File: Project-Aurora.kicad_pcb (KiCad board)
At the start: 4 copper layers, 285 x 94.6 mm, 252 parts, among them P1 USB_OTG, P2 FLASH_HDR, SW1 Reset, SW10 SW_PUSH, SW11 SW_PUSH, SW12 SW_PUSH, SW13 SW_PUSH, SW14 SW_PUSH, SW15 SW_PUSH, SW16 SW_PUSH, SW17 SW_PUSH, SW18 SW_PUSH, SW19 SW_PUSH, SW2 SW_PUSH, SW20 SW_PUSH, SW21 SW_PUSH, SW22 SW_PUSH, SW23 SW_PUSH, SW24 SW_PUSH, SW25 SW_PUSH, SW26 SW_PUSH, SW27 SW_PUSH, SW28 SW_PUSH, SW29 SW_PUSH, SW3 SW_PUSH, SW30 SW_PUSH, SW31 SW_PUSH, SW32 SW_PUSH, SW33 SW_PUSH, SW34 SW_PUSH, SW35 SW_PUSH, SW36 SW_PUSH, SW37 SW_PUSH, SW38 SW_PUSH, SW39 SW_PUSH, SW4 SW_PUSH, SW40 SW_PUSH, SW41 SW_PUSH, SW42 SW_PUSH, SW43 SW_PUSH, SW44 SW_PUSH, SW45 SW_PUSH, SW46 SW_PUSH, SW47 SW_PUSH, SW48 SW_PUSH, SW49 SW_PUSH, SW5 SW_PUSH, SW50 SW_PUSH, SW51 SW_PUSH, SW52 SW_PUSH, SW53 SW_PUSH, SW54 SW_PUSH, SW55 SW_PUSH, SW56 SW_PUSH, SW57 SW_PUSH, SW58 SW_PUSH, SW59 SW_PUSH, SW6 SW_PUSH, SW60 SW_PUSH, SW61 SW_PUSH, SW62 SW_PUSH, SW63 SW_PUSH, SW64 SW_PUSH, SW65 SW_PUSH, SW66 SW_PUSH, SW7 SW_PUSH, SW8 SW_PUSH, SW9 SW_PUSH, U1 IS31FL3732, U2 Freescale_K20P64M72SF1, U3 TPS62086, U5 IS31FL3732, U6 Case-Ground, X1 CRYSTAL_SMD

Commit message: Optimised Routing of Ground Trace
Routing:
- net GND: track 340.4 -> 322.8 mm, vias 37 -> 36
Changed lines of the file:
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@@
     (links 613)
     (no_connects 0)
-    (area 62.241349 64.570349 347.341251 159.269751)
+    (area -446.689481 14.894801 665.190441 593.940901)
     (thickness 1.6002)
     (drawings 3816)
-    (tracks 2868)
+    (tracks 2870)
     (zones 0)
     (modules 252)
@@
   )
   (setup
-    (last_trace_width 0.4064)
+    (last_trace_width 0.889)
     (user_trace_width 0.19)
     (user_trace_width 0.254)
@@
   (segment (start 159.004 146.696) (end 161.544 146.696) (width 0.4064) (layer Back) (net 1) (status 30))
   (segment (start 161.544 146.696) (end 164.084 146.696) (width 0.4064) (layer Back) (net 1) (status 30))
+  (segment (start 88.646 152.654) (end 96.266 152.654) (width 0.889) (layer Back) (net 2))
+  (segment (start 98.552 154.94) (end 105.664 154.94) (width 0.889) (layer Back) (net 2))
+  (segment (start 96.266 152.654) (end 98.552 154.94) (width 0.889) (layer Back) (net 2))
+  (segment (start 66.548 126.492) (end 66.548 135.128) (width 0.889) (layer Back) (net 2))
+  (segment (start 76.2 140.208) (end 88.646 152.654) (width 0.889) (layer Back) (net 2))
+  (segment (start 71.628 140.208) (end 76.2 140.208) (width 0.889) (layer Back) (net 2))
+  (segment (start 66.548 135.128) (end 71.628 140.208) (width 0.889) (layer Back) (net 2))
   (segment (start 98.552 115.758) (end 94.93 115.758) (width 0.19) (layer Back) (net 2) (status 10))
   (segment (start 90.932 116.84) (end 90.932 117.348) (width 0.19) (layer Back) (net 2))
@@
   (segment (start 108.712 154.94) (end 107.188 154.94) (width 0.19) (layer Front) (net 2))
   (via (at 107.188 154.94) (size 1) (drill 0.4) (layers Front Back) (net 2))
-  (via (at 105.664 154.94) (size 1) (drill 0.4) (layers Front Back) (net 2))
-  (segment (start 64.008 155.448) (end 66.04 157.48) (width 0.889) (layer Back) (net 2))
-  (segment (start 66.04 157.48) (end 103.124 157.48) (width 0.889) (layer Back) (net 2))
-  (segment (start 105.664 154.94) (end 103.124 157.48) (width 0.889) (layer Back) (net 2))
-  (segment (start 64.008 129.032) (end 64.008 155.448) (width 0.889) (layer Back) (net 2))
-  (segment (start 70.104 122.936) (end 64.008 129.032) (width 0.889) (layer Back) (net 2))
+  (segment (start 70.104 122.936) (end 66.548 126.492) (width 0.889) (layer Back) (net 2))
   (segment (start 70.104 118.872) (end 70.104 122.936) (width 0.889) (layer Back) (net 2))
   (segment (start 107.188 154.94) (end 105.664 154.94) (width 0.19) (layer Back) (net 2))

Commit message: Prevented potential Ground loop
On the Shielding of the USB Connecor
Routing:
- net GNDPWR: track 36.7 -> 25.5 mm
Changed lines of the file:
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@@
   (general
     (links 613)
-    (no_connects 0)
-    (area -446.689481 14.894801 665.190441 593.940901)
+    (no_connects 3)
+    (area 62.241349 64.570349 347.341251 159.269751)
     (thickness 1.6002)
     (drawings 3816)
-    (tracks 2870)
+    (tracks 2865)
     (zones 0)
     (modules 252)
@@
   )
   (setup
-    (last_trace_width 0.889)
+    (last_trace_width 0.4064)
     (user_trace_width 0.19)
     (user_trace_width 0.254)
@@
     (mod_text_size 1.524 1.524)
     (mod_text_width 0.3048)
-    (pad_size 0.9 0.9)
-    (pad_drill 0.9)
+    (pad_size 1.55 1)
+    (pad_drill 1.15)
     (pad_to_mask_clearance 0.1016)
     (pad_to_paste_clearance -0.02)
@@
     (pad 5 smd rect (at 1.2991 1.56254 270) (size 1.35 0.4) (layers Back B.Paste B.Mask)
       (net 2 GND))
-    (pad 6 thru_hole oval (at -2.5009 1.56254 270) (size 0.95 1.25) (drill oval 0.55 0.85) (layers *.Cu *.Mask B.SilkS)
-      (net 166 GNDPWR))
+    (pad 6 thru_hole oval (at -2.5009 1.56254 270) (size 0.95 1.25) (drill oval 0.55 0.85) (layers *.Cu *.Mask B.SilkS))
     (pad 6 thru_hole oval (at 2.4991 1.56254 270) (size 0.95 1.25) (drill oval 0.55 0.85) (layers *.Cu *.Mask B.SilkS)
       (net 166 GNDPWR))
-    (pad 6 thru_hole oval (at -3.5009 -1.13746 270) (size 1.55 1) (drill oval 1.15 0.5) (layers *.Cu *.Mask B.SilkS)
-      (net 166 GNDPWR))
-    (pad 6 thru_hole oval (at 3.4991 -1.13746 270) (size 1.55 1) (drill oval 1.15 0.5) (layers *.Cu *.Mask B.SilkS)
-      (net 166 GNDPWR))
+    (pad 6 thru_hole oval (at -3.5009 -1.13746 270) (size 1.55 1) (drill oval 1.15 0.5) (layers *.Cu *.Mask B.SilkS))
+    (pad 6 thru_hole oval (at 3.4991 -1.13746 270) (size 1.55 1) (drill oval 1.15 0.5) (layers *.Cu *.Mask B.SilkS))
   )
   (module mx2a:KSEM31GLFS (layer Back)
@@
   (segment (start 229.656 147.844) (end 226.142 147.844) (width 0.19) (layer Back) (net 164) (status 10))
   (segment (start 229.706 147.844) (end 229.656 147.844) (width 0.19) (layer Back) (net 164) (status 30))
-  (segment (start 78.0171 67.1725) (end 77.0171 66.1725) (width 0.889) (layer In1.Cu) (net 166) (status 20))
-  (segment (start 78.0171 68.8725) (end 78.0171 67.1725) (width 0.889) (layer In1.Cu) (net 166) (status 10))
-  (segment (start 83.0171 68.8725) (end 78.0171 68.8725) (width 0.889) (layer In1.Cu) (net 166) (status 30))
   (segment (start 83.0171 80.9851) (end 83.0171 68.8725) (width 0.889) (layer In1.Cu) (net 166) (status 20))
   (segment (start 87.4878 85.4558) (end 83.0171 80.9851) (width 0.889) (layer In1.Cu) (net 166))
   (segment (start 87.4878 92.522) (end 87.4878 85.4558) (width 0.889) (layer In1.Cu) (net 166) (status 10))
-  (segment (start 83.0171 67.1725) (end 84.0171 66.1725) (width 0.889) (layer In1.Cu) (net 166) (status 20))
-  (segment (start 83.0171 68.8725) (end 83.0171 67.1725) (width 0.889) (layer In1.Cu) (net 166) (status 10))
   (segment (start 172.452 147.444) (end 171.704 146.696) (width 0.19) (layer Back) (net 167) (status 20))
   (segment (start 173.776 147.444) (end 172.452 147.444) (width 0.19) (layer Back) (net 167) (status 10))

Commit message: Added Fiducials, i2c Testpoints and a Filter-Cap
Fiducials: 4 Two-Sided feducials in the Corners, 4 Feducials on the Back near the ICs (these might be Overkill)
i2c Testpoints: Makes debugging less of a hassle, also tuned track-lengths of SCL and SDA
Filter-Cap: Supposed to prevent high-pitched buzzing during load
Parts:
- added C20: 100uF, Capacitors_SMD:C_0805, B.Cu at (79.0, 75.9)
- added FID1: Nothing-to-see-here, Fiducials:Fiducial_1mm_Dia_2.54mm_Outer_CopperTop, F.Cu at (90.4, 83.8)
- added FID10: Nothing-to-see-here, Fiducials:Fiducial_1mm_Dia_2.54mm_Outer_CopperBottom, F.Cu at (156.5, 152.4)
- added FID11: Nothing-to-see-here, Fiducials:Fiducial_1mm_Dia_2.54mm_Outer_CopperBottom, F.Cu at (217.4, 154.9)
- added FID12: Nothing-to-see-here, Fiducials:Fiducial_1mm_Dia_2.54mm_Outer_CopperBottom, F.Cu at (240.3, 139.7)
- added FID2: Nothing-to-see-here, Fiducials:Fiducial_1mm_Dia_2.54mm_Outer_CopperBottom, F.Cu at (90.4, 83.8)
- added FID3: Nothing-to-see-here, Fiducials:Fiducial_1mm_Dia_2.54mm_Outer_CopperTop, F.Cu at (341.9, 71.1)
- added FID4: Nothing-to-see-here, Fiducials:Fiducial_1mm_Dia_2.54mm_Outer_CopperBottom, F.Cu at (341.9, 71.1)
- added FID5: Nothing-to-see-here, Fiducials:Fiducial_1mm_Dia_2.54mm_Outer_CopperTop, F.Cu at (322.8, 151.1)
- added FID6: Nothing-to-see-here, Fiducials:Fiducial_1mm_Dia_2.54mm_Outer_CopperBottom, F.Cu at (322.8, 151.1)
- added FID7: Nothing-to-see-here, Fiducials:Fiducial_1mm_Dia_2.54mm_Outer_CopperTop, F.Cu at (87.9, 144.8)
- added FID8: Nothing-to-see-here, Fiducials:Fiducial_1mm_Dia_2.54mm_Outer_CopperBottom, F.Cu at (87.9, 144.8)
- added FID9: Nothing-to-see-here, Fiducials:Fiducial_1mm_Dia_2.54mm_Outer_CopperBottom, F.Cu at (143.8, 139.7)
- added W1: TEST, Connect:PINHEAD1-2, F.Cu at (207.3, 150.4)
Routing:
- net /SCL: track 109.3 -> 112.8 mm
- net /SDA: track 108.8 -> 112.1 mm
- net GND: track 322.8 -> 323.9 mm
- net /5V: track 69.6 -> 70.8 mm

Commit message: Forgot some Stuff in the last Commit
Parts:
- D1, D10, D11, D12, D129, D13, D130, D131, D14, D15, D16, D17, D18, D19, D2, D20, D21, D22, D23, D24, D25, D26, D27, D28, D29, D3, D30, D31, D32, D33, D34, D35, D36, D37, D38, D39, D4, D40, D41, D42, D43, D44, D45, D46, D47, D48, D49, D5, D50, D51, D52, D53, D54, D55, D56, D57, D58, D59, D6, D60, D61, D62, D63, D64, D7, D8, D9: footprint mx2a:RGB -> Keyboard_Stuff:RGB
- D100, D101, D102, D103, D104, D105, D106, D107, D108, D109, D110, D111, D112, D113, D114, D115, D116, D117, D118, D119, D120, D121, D122, D123, D124, D126, D127, D128, D65, D66, D67, D68, D69, D70, D71, D72, D73, D74, D75, D76, D77, D78, D79, D80, D81, D82, D83, D84, D85, D86, D87, D88, D89, D90, D91, D92, D93, D94, D95, D96, D97, D98, D99: footprint mx2a:SOD-123 -> Keyboard_Stuff:SOD-123
- P2: footprint mx2a:JLINK_NEEDLE -> Keyboard_Stuff:JLINK_NEEDLE
- SW1: footprint mx2a:KSEM31GLFS -> Keyboard_Stuff:KSEM31GLFS
- SW10, SW11, SW12, SW13, SW14, SW15, SW16, SW17, SW18, SW19, SW2, SW20, SW21, SW22, SW23, SW24, SW25, SW26, SW27, SW28, SW29, SW3, SW30, SW31, SW32, SW33, SW34, SW35, SW36, SW37, SW38, SW39, SW4, SW40, SW41, SW42, SW43, SW44, SW45, SW46, SW47, SW48, SW49, SW5, SW50, SW51, SW52, SW53, SW54, SW55, SW56, SW57, SW58, SW59, SW6, SW60, SW61, SW62, SW63, SW64, SW65, SW66, SW7, SW8, SW9: footprint mx2a:MX1A -> Keyboard_Stuff:MX1A
- U2: value Freescale_K20P64M72SF1 -> MK20DX256VLH7
- U3: footprint mx2a:VSON-7 -> Keyboard_Stuff:VSON-7
- U6: footprint mx2a:PKRHC -> Keyboard_Stuff:PKRHC
- renumbered U5 to U4
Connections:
- net /USB-D+ renamed Net-(P1-Pad3)
- net /USB-D- renamed Net-(P1-Pad2)
- U2 pad 19: (no net) -> Net-(U2-Pad19)

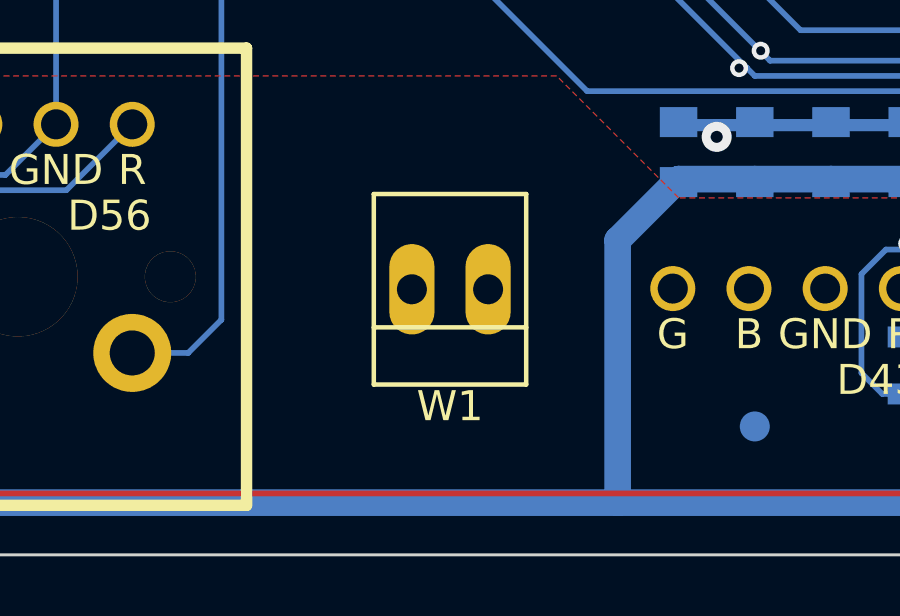
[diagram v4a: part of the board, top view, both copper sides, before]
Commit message: Picked more appropriate i2c Debug Port
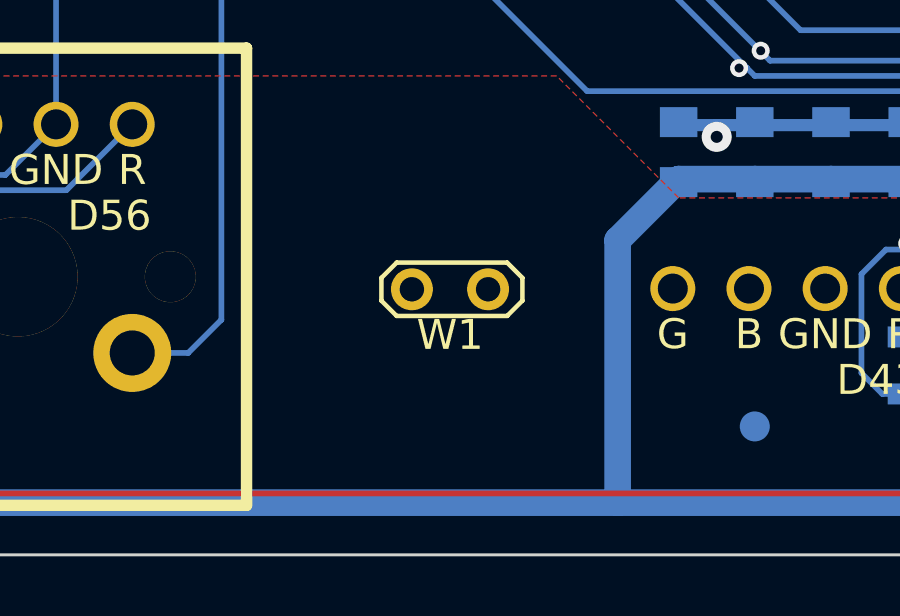
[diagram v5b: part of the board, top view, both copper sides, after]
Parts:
- W1: footprint Connect:PINHEAD1-2 -> Measurement_Points:Test_Point_2Pads
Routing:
- net /SCL: track 112.8 -> 112.2 mm
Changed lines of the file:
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@@
     )
   )
-  (module Connect:PINHEAD1-2 (layer Front)
-    (at 207.264 150.368 180)
-    (attr virtual)
-    (fp_text reference W1 (at 0 -3.9 180) (layer F.SilkS)
-      (effects (font (size 1 1) (thickness 0.15)))
-    )
-    (fp_text value TEST (at 0 3.81 180) (layer F.Fab)
-      (effects (font (size 1 1) (thickness 0.15)))
-    )
-    (fp_line (start 2.54 -1.27) (end -2.54 -1.27) (layer F.SilkS) (width 0.15))
-    (fp_line (start 2.54 3.175) (end -2.54 3.175) (layer F.SilkS) (width 0.15))
-    (fp_line (start -2.54 -3.175) (end 2.54 -3.175) (layer F.SilkS) (width 0.15))
-    (fp_line (start -2.54 -3.175) (end -2.54 3.175) (layer F.SilkS) (width 0.15))
-    (fp_line (start 2.54 -3.175) (end 2.54 3.175) (layer F.SilkS) (width 0.15))
-    (pad 1 thru_hole oval (at -1.27 0 180) (size 1.50622 3.01498) (drill 0.99822) (layers *.Cu *.Mask)
-      (net 72 /SDA))
-    (pad 2 thru_hole oval (at 1.27 0 180) (size 1.50622 3.01498) (drill 0.99822) (layers *.Cu *.Mask)
-      (net 71 /SCL))
-  )
   (module Keyboard_Stuff:RGB (layer Front)
     (at 326.212 111.85 180)
@@
     )
   )
+  (module Measurement_Points:Test_Point_2Pads (layer Front)
+    (at 207.264 150.368 180)
+    (descr "Connecteurs 2 pins")
+    (tags "CONN DEV")
+    (fp_text reference W1 (at 0 -1.524 180) (layer F.SilkS)
+      (effects (font (size 1 1) (thickness 0.15)))
+    )
+    (fp_text value TEST (at 0.127 1.524 180) (layer F.Fab)
+      (effects (font (size 1 1) (thickness 0.15)))
+    )
+    (fp_line (start -1.905 -0.889) (end 1.778 -0.889) (layer F.SilkS) (width 0.15))
+    (fp_line (start 1.778 -0.889) (end 2.286 -0.381) (layer F.SilkS) (width 0.15))
+    (fp_line (start 2.286 -0.381) (end 2.286 0.381) (layer F.SilkS) (width 0.15))
+    (fp_line (start 2.286 0.381) (end 1.778 0.889) (layer F.SilkS) (width 0.15))
+    (fp_line (start 1.778 0.889) (end -1.905 0.889) (layer F.SilkS) (width 0.15))
+    (fp_line (start -1.905 0.889) (end -2.413 0.381) (layer F.SilkS) (width 0.15))
+    (fp_line (start -2.413 0.381) (end -2.413 -0.381) (layer F.SilkS) (width 0.15))
+    (fp_line (start -2.413 -0.381) (end -1.905 -0.889) (layer F.SilkS) (width 0.15))
+    (pad 1 thru_hole circle (at -1.27 0 180) (size 1.397 1.397) (drill 0.8128) (layers *.Cu *.Mask F.SilkS)
+      (net 72 /SDA))
+    (pad 2 thru_hole circle (at 1.27 0 180) (size 1.397 1.397) (drill 0.8128) (layers *.Cu *.Mask F.SilkS)
+      (net 71 /SCL))
+  )
   (gr_line (start 150.368 150.749) (end 150.622 150.749) (angle 90) (layer B.SilkS) (width 0.381))
   (gr_line (start 150.368 151.003) (end 150.368 150.749) (angle 90) (layer B.SilkS) (width 0.381))
@@
   (segment (start 224.79 150.114) (end 223.012 151.892) (width 0.19) (layer In1.Cu) (net 71))
   (segment (start 223.012 151.892) (end 212.852 151.892) (width 0.19) (layer In1.Cu) (net 71))
-  (segment (start 212.852 151.892) (end 209.296 148.336) (width 0.19) (layer In1.Cu) (net 71))
-  (segment (start 209.296 148.336) (end 207.772 148.336) (width 0.19) (layer In1.Cu) (net 71))
-  (segment (start 207.772 148.336) (end 205.994 150.114) (width 0.19) (layer In1.Cu) (net 71) (status 20))
+  (segment (start 212.852 151.892) (end 210.058 149.098) (width 0.19) (layer In1.Cu) (net 71))
+  (segment (start 210.058 149.098) (end 207.01 149.098) (width 0.19) (layer In1.Cu) (net 71))
+  (segment (start 207.01 149.098) (end 205.994 150.114) (width 0.19) (layer In1.Cu) (net 71) (status 20))
   (segment (start 205.994 150.114) (end 205.994 150.356) (width 0.19) (layer In1.Cu) (net 71) (status 30))
   (segment (start 205.994 150.356) (end 205.994 150.368) (width 0.19) (layer In1.Cu) (net 71) (status 30))
@@
   (segment (start 188.872 153.012) (end 191.112 153.012) (width 0.19) (layer In1.Cu) (net 72))
   (segment (start 191.112 153.012) (end 193.144 155.044) (width 0.19) (layer In1.Cu) (net 72))
-  (segment (start 193.144 155.044) (end 206.652 155.044) (width 0.19) (layer In1.Cu) (net 72))
-  (segment (start 206.652 155.044) (end 208.534 153.162) (width 0.19) (layer In1.Cu) (net 72))
-  (segment (start 208.534 153.162) (end 208.534 150.368) (width 0.19) (layer In1.Cu) (net 72) (status 20))
+  (segment (start 193.144 155.044) (end 206.144 155.044) (width 0.19) (layer In1.Cu) (net 72))
+  (segment (start 206.144 155.044) (end 208.534 152.654) (width 0.19) (layer In1.Cu) (net 72))
+  (segment (start 208.534 152.654) (end 208.534 150.368) (width 0.19) (layer In1.Cu) (net 72) (status 800020))
   (segment (start 208.534 150.368) (end 210.312 150.368) (width 0.19) (layer In1.Cu) (net 72) (status 10))
   (segment (start 212.344 152.4) (end 224.028 152.4) (width 0.19) (layer In1.Cu) (net 72))
